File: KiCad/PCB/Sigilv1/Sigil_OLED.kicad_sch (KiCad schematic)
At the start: 3 parts, among them J2 INLAND 1.3" OLED HEADER (7-PI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, J3 BUZZER LOGICAL ONLY, U1 REMOVABLE ESP32 DEVKIT / 2 x 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

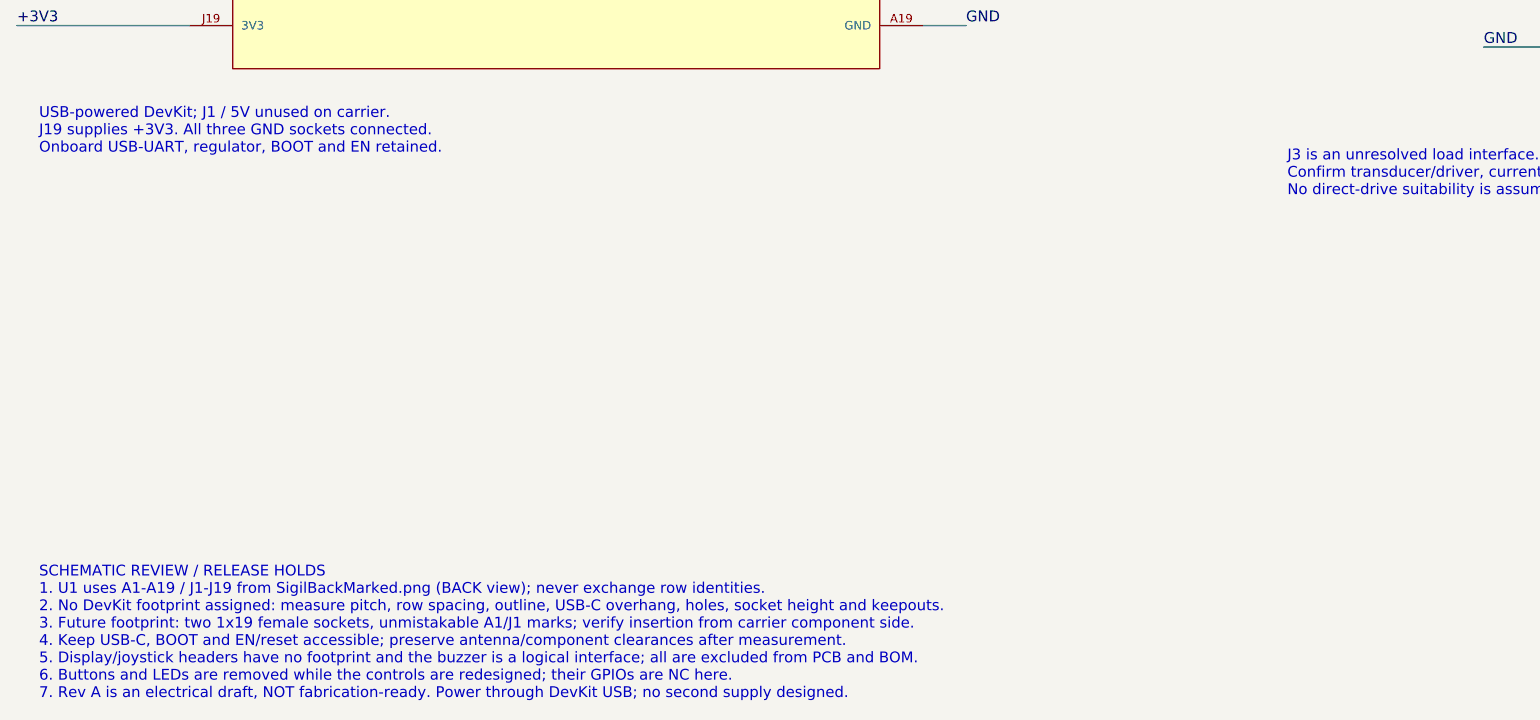
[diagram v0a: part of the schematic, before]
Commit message: Sigil-rendered status light, Jewel ring, BOOT Pair; louder Atlas speaker
- LedState (packet 25, CAPABILITY_LED_STATE 0x20): Atlas sends the light's
  meaning (cue, overlays, seat, style, anchor age) once per change and on
  every Hello; the Sigil renders it (sigil_led.cpp) to an RGB LED (PWM on
  all pins) and, on the E-ink build, spatially on a NeoPixel Jewel 7 RGBW
  (Adafruit NeoPixel 1.15.5, GPIO26). Legacy SetRed/Green/Blue kept.
  LedCue/LedOverlay move to protocol.h.
- Pair is the DevKit BOOT button (GPIO0) on both hardware builds; Wokwi
  keeps GPIO19.
- Atlas speaker: LEDC square wave, volume steps ~1/2, 3/4, full.
- E-ink schematic gains J5 (Jewel) and R1; verifier checks the ring pin.
- Sigil 0.6.0-dev; host tests for the renderer and LedState transport.

Co-Authored-By: Claude Opus 5.5 <noreply@anthropic.com>
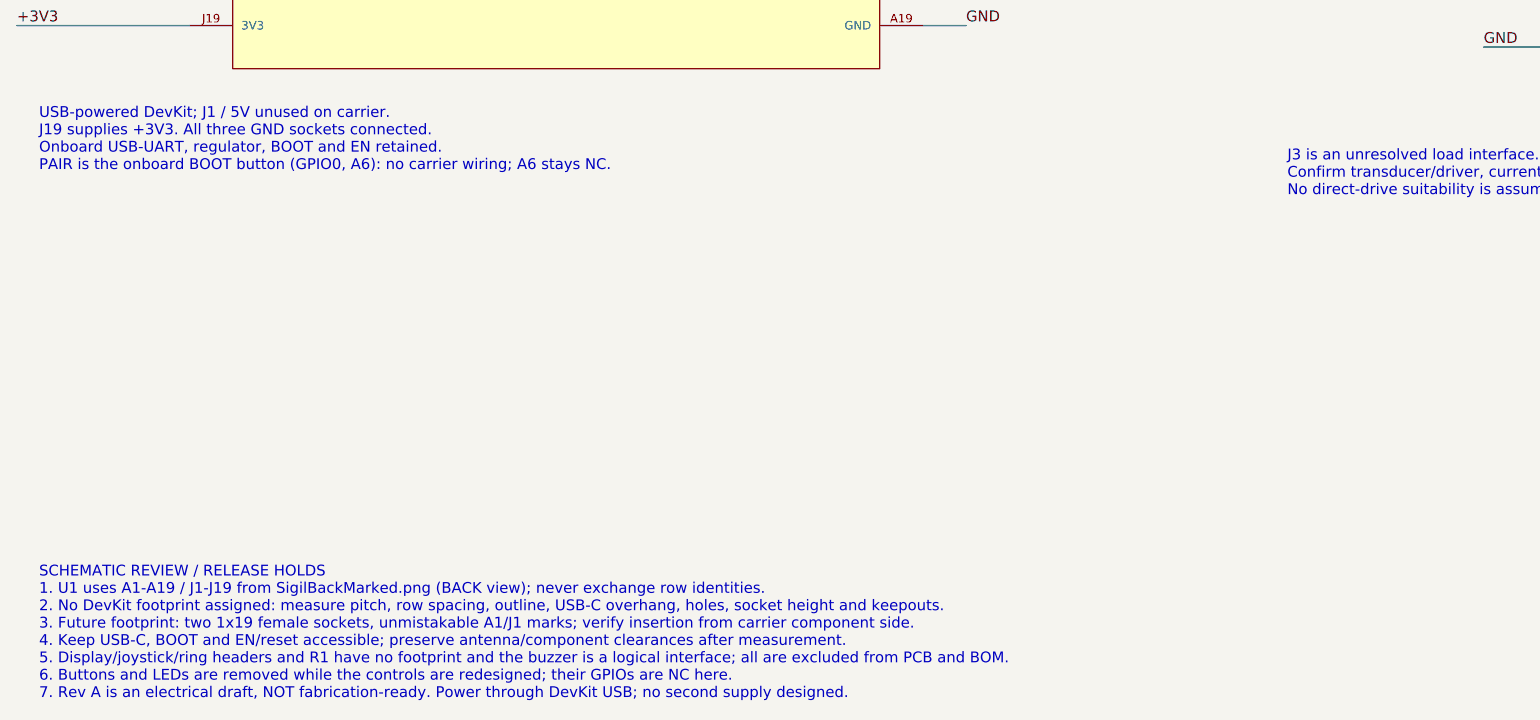
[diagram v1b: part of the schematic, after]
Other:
- note added: "USB-powered DevKit; J1 / 5V unused on carrier. J19 supplies +3V3. All three GND sockets connected. Onboard USB-UART, regulator, BOOT and EN retained. PAIR is the onboard BOOT button (GPIO0, A6): no carrier wiring; A6 stays NC."
- note removed: "USB-powered DevKit; J1 / 5V unused on carrier. J19 supplies +3V3. All three GND sockets connected. Onboard USB-UART, regulator, BOOT and EN retained."
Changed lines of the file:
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@@
 		)
 	)
-	(text "USB-powered DevKit; J1 / 5V unused on carrier.\nJ19 supplies +3V3. All three GND sockets connected.\nOnboard USB-UART, regulator, BOOT and EN retained."
+	(text "USB-powered DevKit; J1 / 5V unused on carrier.\nJ19 supplies +3V3. All three GND sockets connected.\nOnboard USB-UART, regulator, BOOT and EN retained.\nPAIR is the onboard BOOT button (GPIO0, A6): no carrier wiring; A6 stays NC."
 		(exclude_from_sim no)
 		(at 28 157 0)
@@
 			(font
 				(size 1.5 1.5)
+			)
+			(justify left top)
+		)
+	)
+	(text "SCHEMATIC REVIEW / RELEASE HOLDS\n1. U1 uses A1-A19 / J1-J19 from SigilBackMarked.png (BACK view); never exchange row identities.\n2. No DevKit footprint assigned: measure pitch, row spacing, outline, USB-C overhang, holes, socket height and keepouts.\n3. Future footprint: two 1x19 female sockets, unmistakable A1/J1 marks; verify insertion from carrier component side.\n4. Keep USB-C, BOOT and EN/reset accessible; preserve antenna/component clearances after measurement.\n5. Display/joystick/ring headers and R1 have no footprint and the buzzer is a logical interface; all are excluded from PCB and BOM.\n6. Buttons and LEDs are removed while the controls are redesigned; their GPIOs are NC here.\n7. Rev A is an electrical draft, NOT fabrication-ready. Power through DevKit USB; no second supply designed."
+		(exclude_from_sim no)
+		(at 28 211 0)
+		(effects
+			(font
+				(size 1.27 1.27)
 			)
 			(justify left top)
@@
 			)
 			(justify left top)
-		)
-	)
-	(text "SCHEMATIC REVIEW / RELEASE HOLDS\n1. U1 uses A1-A19 / J1-J19 from SigilBackMarked.png (BACK view); never exchange row identities.\n2. No DevKit footprint assigned: measure pitch, row spacing, outline, USB-C overhang, holes, socket height and keepouts.\n3. Future footprint: two 1x19 female sockets, unmistakable A1/J1 marks; verify insertion from carrier component side.\n4. Keep USB-C, BOOT and EN/reset accessible; preserve antenna/component clearances after measurement.\n5. Display/joystick headers have no footprint and the buzzer is a logical interface; all are excluded from PCB and BOM.\n6. Buttons and LEDs are removed while the controls are redesigned; their GPIOs are NC here.\n7. Rev A is an electrical draft, NOT fabrication-ready. Power through DevKit USB; no second supply designed."
-		(exclude_from_sim no)
-		(at 28 211 0)
-		(effects
-			(font
-				(size 1.27 1.27)
-			)
-			(justify left top)
